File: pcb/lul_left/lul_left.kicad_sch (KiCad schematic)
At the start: 54 parts, among them J1 SWD_Ext, J2 Conn_02x04_Odd_Even, SW1 SW_Push, SW10 SW_Push, SW11 SW_Push, SW12 SW_Push, SW13 SW_Push, SW14 SW_Push, SW15 SW_Push, SW16 SW_Push, SW17 SW_Push, SW18 SW_DPDT_x2, SW19 SW_RESET, SW2 SW_Push, SW20 SW_DPDT_x2, SW3 SW_Push, SW4 SW_Push, SW5 SW_Push, SW6 SW_Push, SW7 SW_Push, SW8 SW_Push, SW9 SW_Push, U1 E73-2G4M08S1C, U2 XC6206PxxxMR, U3 DW01A, U4 FS8205, Y1 Crystal_Small

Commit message: added libraries and a few edits to schematic
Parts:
- removed ENC1: Encoder, weteor:Mitsumi_SIQ-02FVS3, symbol Connector_Generic:Conn_01x04
- D1, D10, D11, D12, D13, D14, D15, D16, D17, D2, D3, D4, D5, D6, D7, D8, D9: footprint weteor:D_SOD-123 -> Diode_SMD:D_SOD-123
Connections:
- net ENC_A: no longer names the net of U1.10 (P0.30/AIN6*)
- net ENC_B: no longer names the net of U1.8 (P0.29/AIN5*)
- net ENC_S: no longer names the net of U1.9 (P0.31/AIN7*)

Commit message: remove submodules
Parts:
- SW1, SW10, SW11, SW12, SW13, SW14, SW15, SW16, SW17, SW2, SW3, SW4, SW5, SW6, SW7, SW9: footprint weteor:ChocV1_V2_Hotswap_3d -> MX_Only:MXOnly-1U-Hotswap
- SW18, SW20: footprint weteor:DPDT - C2837066 -> MX_Only:MXOnly-1U-Hotswap
- SW19: footprint weteor:Micro_Push_Button_3x6x2.5mm -> MX_Only:MXOnly-1U-Hotswap
- SW8: footprint weteor:ChocV1_V2_Hotswap_1.5u -> MX_Only:MXOnly-1U-Hotswap
- U1: footprint weteor:E73-2G4M08S1C_bottom -> MX_Only:MXOnly-1U-Hotswap
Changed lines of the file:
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@@
       (effects (font (size 1.27 1.27)))
     )
-    (property "Footprint" "weteor:ChocV1_V2_Hotswap_3d" (at 193.675 26.035 0)
+    (property "Footprint" "MX_Only:MXOnly-1U-Hotswap" (at 193.675 26.035 0)
       (effects (font (size 1.27 1.27)) hide)
     )
@@
       (effects (font (size 1.27 1.27)))
     )
-    (property "Footprint" "weteor:ChocV1_V2_Hotswap_3d" (at 212.725 26.035 0)
+    (property "Footprint" "MX_Only:MXOnly-1U-Hotswap" (at 212.725 26.035 0)
       (effects (font (size 1.27 1.27)) hide)
     )
@@
       (effects (font (size 1.27 1.27)))
     )
-    (property "Footprint" "weteor:ChocV1_V2_Hotswap_1.5u" (at 231.775 64.135 0)
+    (property "Footprint" "MX_Only:MXOnly-1U-Hotswap" (at 231.775 64.135 0)
       (effects (font (size 1.27 1.27)) hide)
     )
@@
       (effects (font (size 1.27 1.27)))
     )
-    (property "Footprint" "weteor:ChocV1_V2_Hotswap_3d" (at 231.775 38.735 0)
+    (property "Footprint" "MX_Only:MXOnly-1U-Hotswap" (at 231.775 38.735 0)
       (effects (font (size 1.27 1.27)) hide)
     )
@@
       (effects (font (size 1.27 1.27)))
     )
-    (property "Footprint" "weteor:ChocV1_V2_Hotswap_3d" (at 174.625 38.735 0)
+    (property "Footprint" "MX_Only:MXOnly-1U-Hotswap" (at 174.625 38.735 0)
       (effects (font (size 1.27 1.27)) hide)
     )
@@
       (effects (font (size 1.27 1.27)))
     )
-    (property "Footprint" "weteor:ChocV1_V2_Hotswap_3d" (at 231.775 51.435 0)
+    (property "Footprint" "MX_Only:MXOnly-1U-Hotswap" (at 231.775 51.435 0)
       (effects (font (size 1.27 1.27)) hide)
     )
@@
       (effects (font (size 1.27 1.27)) (justify left))
     )
-    (property "Footprint" "weteor:E73-2G4M08S1C_bottom" (at 87.63 74.93 0)
+    (property "Footprint" "MX_Only:MXOnly-1U-Hotswap" (at 87.63 74.93 0)
       (effects (font (size 1.27 1.27)) hide)
     )
@@
       (effects (font (size 1.27 1.27)))
     )
-    (property "Footprint" "weteor:ChocV1_V2_Hotswap_3d" (at 212.725 38.735 0)
+    (property "Footprint" "MX_Only:MXOnly-1U-Hotswap" (at 212.725 38.735 0)
       (effects (font (size 1.27 1.27)) hide)
     )
@@
       (effects (font (size 1.27 1.27)))
     )
-    (property "Footprint" "weteor:ChocV1_V2_Hotswap_3d" (at 250.825 51.435 0)
+    (property "Footprint" "MX_Only:MXOnly-1U-Hotswap" (at 250.825 51.435 0)
       (effects (font (size 1.27 1.27)) hide)
     )
@@
       (effects (font (size 1.27 1.27)))
     )
-    (property "Footprint" "weteor:DPDT - C2837066" (at 210.82 119.38 0)
+    (property "Footprint" "MX_Only:MXOnly-1U-Hotswap" (at 210.82 119.38 0)
       (effects (font (size 1.27 1.27)) hide)
     )
@@
       (effects (font (size 1.27 1.27)))
     )
-    (property "Footprint" "weteor:ChocV1_V2_Hotswap_3d" (at 250.825 38.735 0)
+    (property "Footprint" "MX_Only:MXOnly-1U-Hotswap" (at 250.825 38.735 0)
       (effects (font (size 1.27 1.27)) hide)
     )
@@
       (effects (font (size 1.27 1.27)))
     )
-    (property "Footprint" "weteor:ChocV1_V2_Hotswap_3d" (at 231.775 26.035 0)
+    (property "Footprint" "MX_Only:MXOnly-1U-Hotswap" (at 231.775 26.035 0)
       (effects (font (size 1.27 1.27)) hide)
     )
@@
       (effects (font (size 1.27 1.27)))
     )
-    (property "Footprint" "weteor:ChocV1_V2_Hotswap_3d" (at 250.825 26.035 0)
+    (property "Footprint" "MX_Only:MXOnly-1U-Hotswap" (at 250.825 26.035 0)
       (effects (font (size 1.27 1.27)) hide)
     )
@@
       (effects (font (size 1.27 1.27)))
     )
-    (property "Footprint" "weteor:ChocV1_V2_Hotswap_3d" (at 250.825 64.135 0)
+    (property "Footprint" "MX_Only:MXOnly-1U-Hotswap" (at 250.825 64.135 0)
       (effects (font (size 1.27 1.27)) hide)
     )
@@
       (effects (font (size 1.27 1.27)) (justify right))
     )
-    (property "Footprint" "weteor:Micro_Push_Button_3x6x2.5mm" (at 33.02 132.08 0)
+    (property "Footprint" "MX_Only:MXOnly-1U-Hotswap" (at 33.02 132.08 0)
       (effects (font (size 1.27 1.27)) hide)
     )
@@
       (effects (font (size 1.27 1.27)))
     )
-    (property "Footprint" "weteor:ChocV1_V2_Hotswap_3d" (at 212.725 51.435 0)
+    (property "Footprint" "MX_Only:MXOnly-1U-Hotswap" (at 212.725 51.435 0)
       (effects (font (size 1.27 1.27)) hide)
     )
@@
       (effects (font (size 1.27 1.27)))
     )
-    (property "Footprint" "weteor:ChocV1_V2_Hotswap_3d" (at 193.675 38.735 0)
+    (property "Footprint" "MX_Only:MXOnly-1U-Hotswap" (at 193.675 38.735 0)
       (effects (font (size 1.27 1.27)) hide)
     )
@@
       (effects (font (size 1.27 1.27)))
     )
-    (property "Footprint" "weteor:ChocV1_V2_Hotswap_3d" (at 174.625 26.035 0)
+    (property "Footprint" "MX_Only:MXOnly-1U-Hotswap" (at 174.625 26.035 0)
       (effects (font (size 1.27 1.27)) hide)
     )
@@
       (effects (font (size 1.27 1.27)))
     )
-    (property "Footprint" "weteor:DPDT - C2837066" (at 210.82 104.775 0)
+    (property "Footprint" "MX_Only:MXOnly-1U-Hotswap" (at 210.82 104.775 0)
       (effects (font (size 1.27 1.27)) hide)
     )
@@
       (effects (font (size 1.27 1.27)))
     )
-    (property "Footprint" "weteor:DPDT - C2837066" (at 189.865 104.775 0)
+    (property "Footprint" "MX_Only:MXOnly-1U-Hotswap" (at 189.865 104.775 0)
       (effects (font (size 1.27 1.27)) hide)
     )
@@
       (effects (font (size 1.27 1.27)))
     )
-    (property "Footprint" "weteor:ChocV1_V2_Hotswap_3d" (at 174.625 51.435 0)
+    (property "Footprint" "MX_Only:MXOnly-1U-Hotswap" (at 174.625 51.435 0)
       (effects (font (size 1.27 1.27)) hide)
     )
@@
       (effects (font (size 1.27 1.27)))
     )
-    (property "Footprint" "weteor:ChocV1_V2_Hotswap_3d" (at 193.675 51.435 0)
-      (effects (font (size 1.27 1.27)) hide)
-    )
+    (property "Footprint" "MX_Only:MXOnly-1U-Hotswap" (at 193.675 51.435 0)
+      (effects (font (size 1.27 1.27)) hide)
+    )

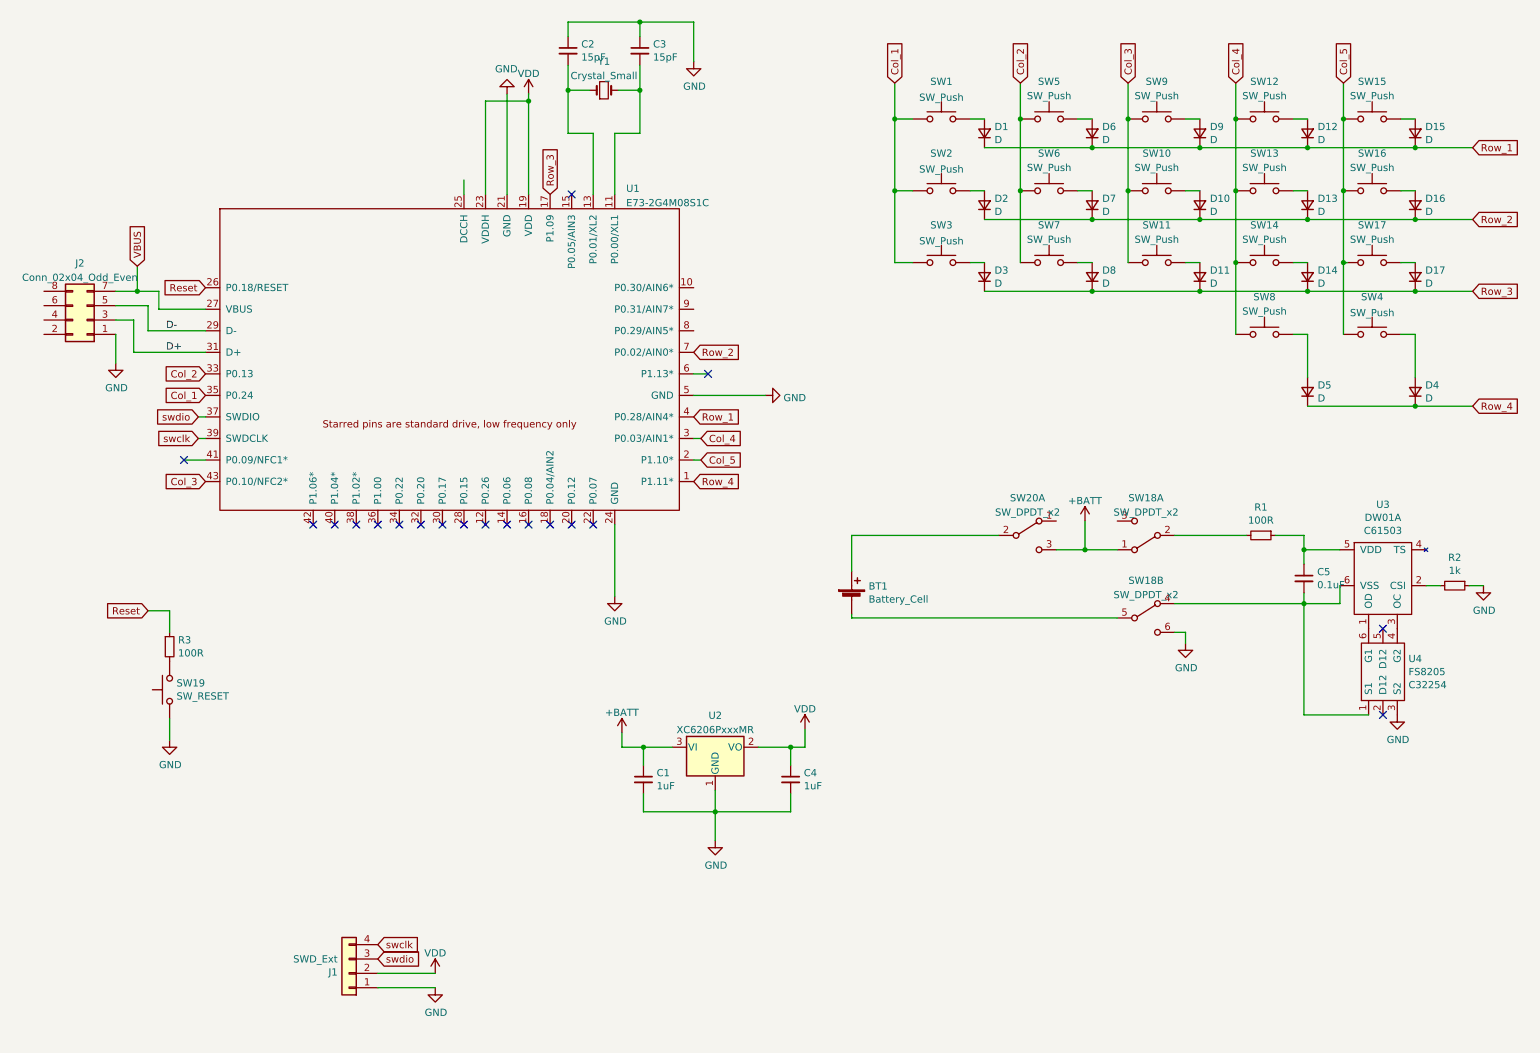
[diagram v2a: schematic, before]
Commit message: Add nice!nano, add on/off switch
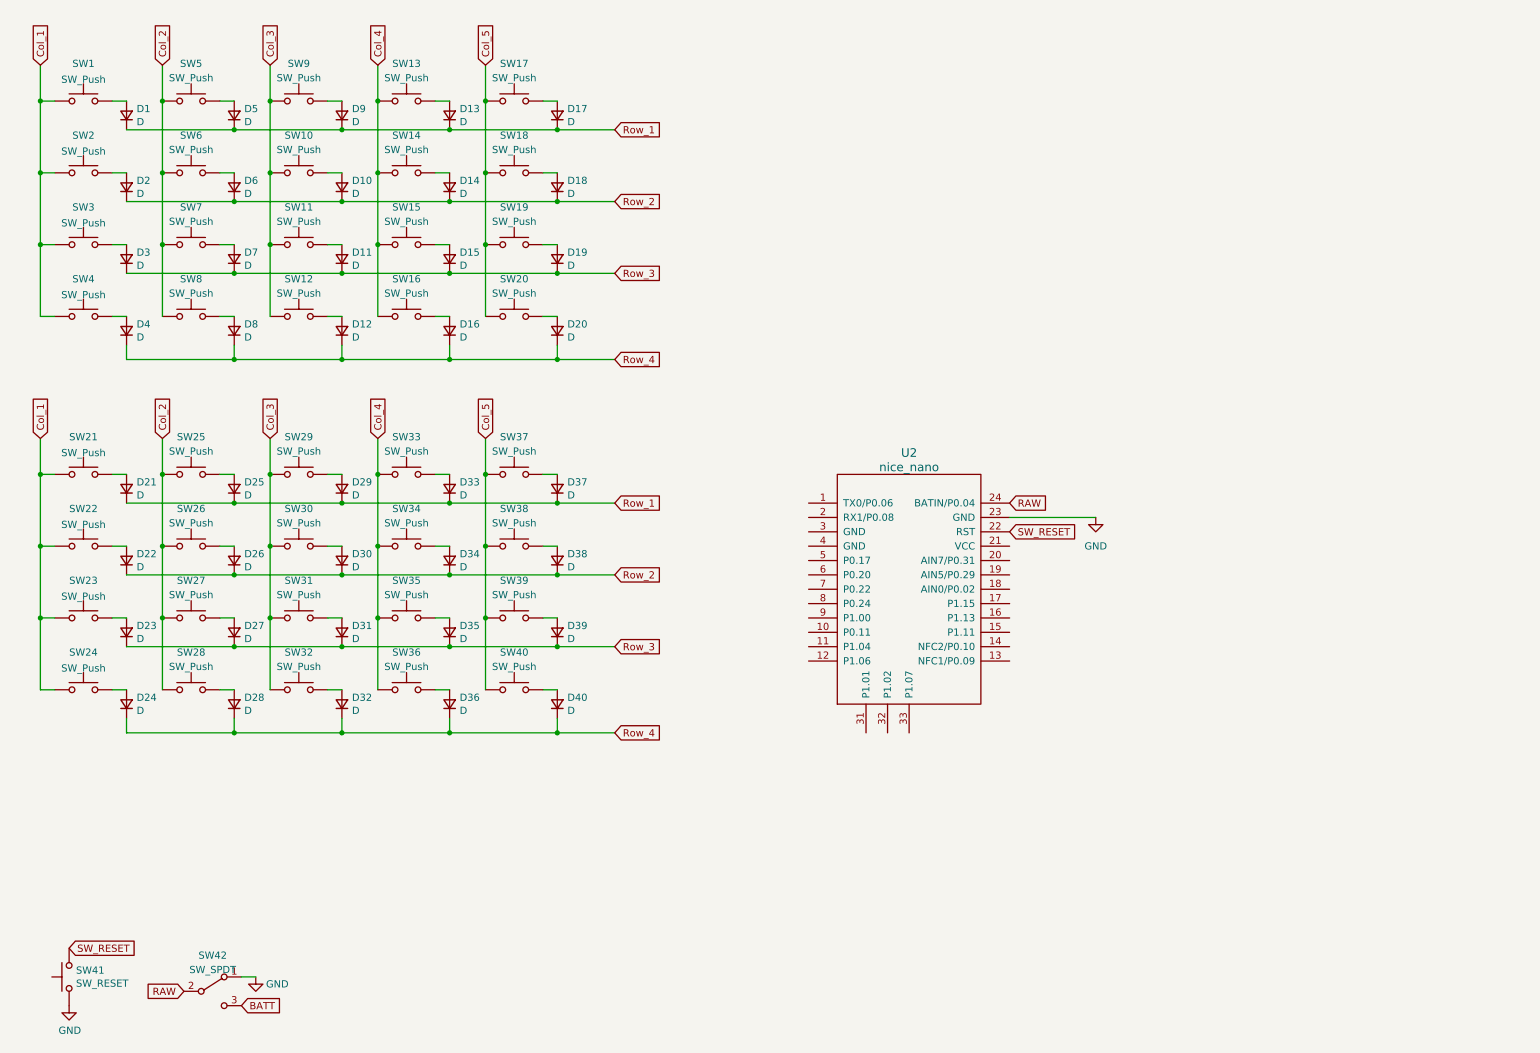
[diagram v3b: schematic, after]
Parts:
- removed BT1: Battery_Cell, weteor:Coin Cell 2032, symbol Device:Battery_Cell
- removed C1, C4: 1uF, Capacitor_SMD:C_0603_1608Metric, symbol Device:C_Small
- removed C2, C3: 15pF, Capacitor_SMD:C_0603_1608Metric, symbol Device:C_Small
- removed C5: 0.1uF, Capacitor_SMD:C_0603_1608Metric, symbol Device:C_Small
- removed J1: SWD_Ext, Connector_PinHeader_2.54mm:PinHeader_1x04_P2.54mm_Vertical, symbol Connector_Generic:Conn_01x04
- removed J2: Conn_02x04_Odd_Even, Connector_PinSocket_1.27mm:PinSocket_2x04_P1.27mm_Vertical, symbol Connector_Generic:Conn_02x04_Odd_Even
- removed R1, R3: 100R, Resistor_SMD:R_0603_1608Metric, symbol Device:R_Small
- removed R2: 1k, Resistor_SMD:R_0603_1608Metric, symbol Device:R_Small
- removed SW18, SW20: SW_DPDT_x2, MX_Only:MXOnly-1U-Hotswap, symbol Switch:SW_DPDT_x2
- removed U1: E73-2G4M08S1C, MX_Only:MXOnly-1U-Hotswap, symbol weteor:E73-2G4M08S1C
- removed U2: XC6206PxxxMR, Package_TO_SOT_SMD:SOT-23, symbol Regulator_Linear:XC6206PxxxMR
- removed U3: DW01A, Package_TO_SOT_SMD:SOT-23-6, symbol le_chiff_ble-rescue:DW01A-kicad-keyboard-parts
- removed U4: FS8205, Package_TO_SOT_SMD:SOT-23-6, symbol le_chiff_ble-rescue:FS8205-kicad-keyboard-parts
- removed Y1: Crystal_Small, Crystal:Crystal_SMD_3215-2Pin_3.2x1.5mm, symbol Device:Crystal_Small
- added D12, D16, D20, D21, D22, D23, D24, D25, D26, D27, D28, D29, D30, D31, D32, D33, D34, D35, D36, D37, D38, D39, D40: D, Diode_SMD:D_SOD-123, symbol Device:D_Small
- added SW18, SW19, SW20, SW21, SW22, SW23, SW24, SW25, SW26, SW27, SW28, SW29, SW30, SW31, SW32, SW33, SW34, SW35, SW36, SW37, SW38, SW39, SW40: SW_Push, zzkeeb:Switch_MX-hotswap, symbol Switch:SW_Push
- added SW42: SW_SPDT, symbol Switch:SW_SPDT
- added U2: nice_nano, symbol nice_nano:nice_nano
- SW1, SW10, SW11, SW12, SW13, SW14, SW15, SW16, SW17, SW2, SW3, SW4, SW5, SW6, SW7, SW8, SW9: footprint MX_Only:MXOnly-1U-Hotswap -> zzkeeb:Switch_MX-hotswap
- SW41: renamed from SW19; footprint MX_Only:MXOnly-1U-Hotswap -> random-keyboard-parts:SKQG-1155865
- renumbered D12 to D15, D15 to D17, D16 to D18, D17 to D19
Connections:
- net Col_1: now also SW4.1, SW21.1, SW22.1, SW23.1, SW24.1
- net Col_2: now also SW8.1, SW25.1, SW26.1, SW27.1, SW28.1
- net Col_3: now also SW12.1, SW29.1, SW30.1, SW31.1, SW32.1
- net Col_4: now also SW15.1, SW16.1, SW33.1, SW34.1, SW35.1, SW36.1; no longer SW12.1, SW8.1
- net Col_5: now also SW18.1, SW19.1, SW20.1, SW37.1, SW38.1, SW39.1, SW40.1; no longer SW15.1, SW16.1, SW4.1
- net GND: now also SW42.1 (A), U2.23 (GND)
- net Row_1: now also D13.1 (K), D5.1 (K), D21.1 (K), D25.1 (K), D29.1 (K), D33.1 (K), D37.1 (K); no longer D15.1 (K), D6.1 (K)
- net Row_2: now also D14.1 (K), D6.1 (K), D22.1 (K), D26.1 (K), D30.1 (K), D34.1 (K), D38.1 (K); no longer D13.1 (K), D7.1 (K)
- net Row_3: now also D15.1 (K), D7.1 (K), D23.1 (K), D27.1 (K), D31.1 (K), D35.1 (K), D39.1 (K); no longer D14.1 (K), D8.1 (K)
- net Row_4: now also D8.1 (K), D12.1 (K), D16.1 (K), D20.1 (K), D24.1 (K), D28.1 (K), D32.1 (K), D36.1 (K), D40.1 (K); no longer D5.1 (K)
- net at SW5.2: now also D5.2 (A); no longer D6.2 (A)
- net at SW8.2: now also D8.2 (A); no longer D5.2 (A)
- net at D19.2 (A): now also SW19.2; no longer SW17.2
- net at SW16.2: now also D16.2 (A); no longer D18.2 (A)
- net at SW12.2: now also D12.2 (A); no longer D15.2 (A)
- net at SW7.2: now also D7.2 (A); no longer D8.2 (A)
- net at D17.2 (A): now also SW17.2; no longer SW15.2
- net SW_RESET: now reaches SW41.2
- net SW_RESET: now also U2.22 (RST)
- net at SW6.2: now also D6.2 (A); no longer D7.2 (A)
- new net: D28.2 (A), SW28.2
- new net: D37.2 (A), SW37.2
- new net: D26.2 (A), SW26.2
- new net: D40.2 (A), SW40.2
- new net: D27.2 (A), SW27.2
- new net: D30.2 (A), SW30.2
- new net: D35.2 (A), SW35.2
- new net: D23.2 (A), SW23.2
- new net: D33.2 (A), SW33.2
- new net: D25.2 (A), SW25.2
- new net: D31.2 (A), SW31.2
- new net: D34.2 (A), SW34.2
- new net: D20.2 (A), SW20.2
- new net: D38.2 (A), SW38.2
- new net: D22.2 (A), SW22.2
- new net: D39.2 (A), SW39.2
- new net: D32.2 (A), SW32.2
- new net: D18.2 (A), SW18.2
- new net: D15.2 (A), SW15.2
- new net: D24.2 (A), SW24.2
- new net: D29.2 (A), SW29.2
- new net: D36.2 (A), SW36.2
- new net: D21.2 (A), SW21.2
- new net BATT: SW42.3 (C)
- new net RAW: SW42.2 (B), U2.24 (BATIN/P0.04)
- no-connect marks 19 -> 0
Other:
- moved on the sheet: D1, D10, D11, D13, D14, D15, D17, D18, D19, D2, D3, D4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
